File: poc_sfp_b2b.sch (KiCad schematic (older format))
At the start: 12 parts, among them J101 Barrel_Jack, Q101 Q_PMOS_DGS, U101 TPS62142

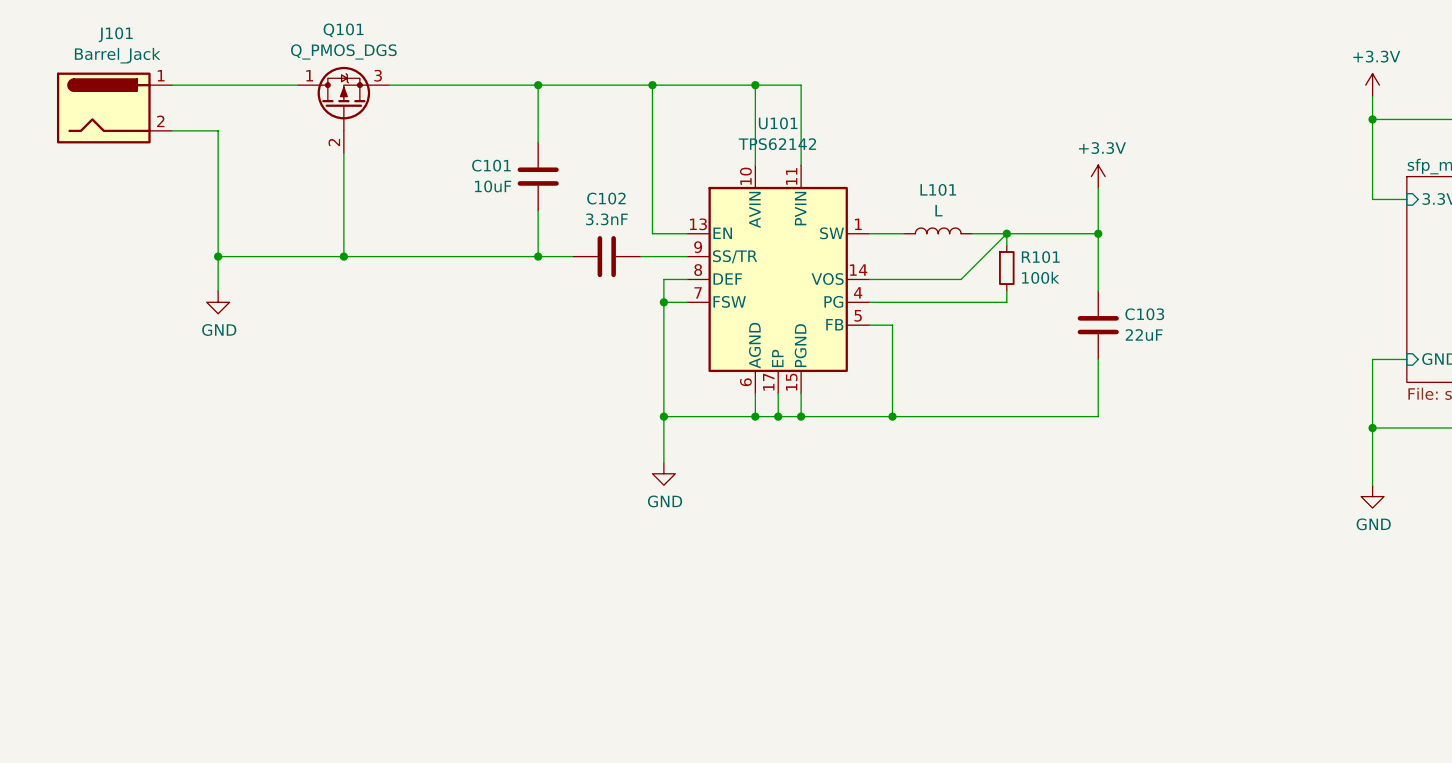
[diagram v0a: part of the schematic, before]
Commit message: fix unconnected tx disable pin
Signed-off-by: Thomas Schmid <tom@binary-kitchen.de>
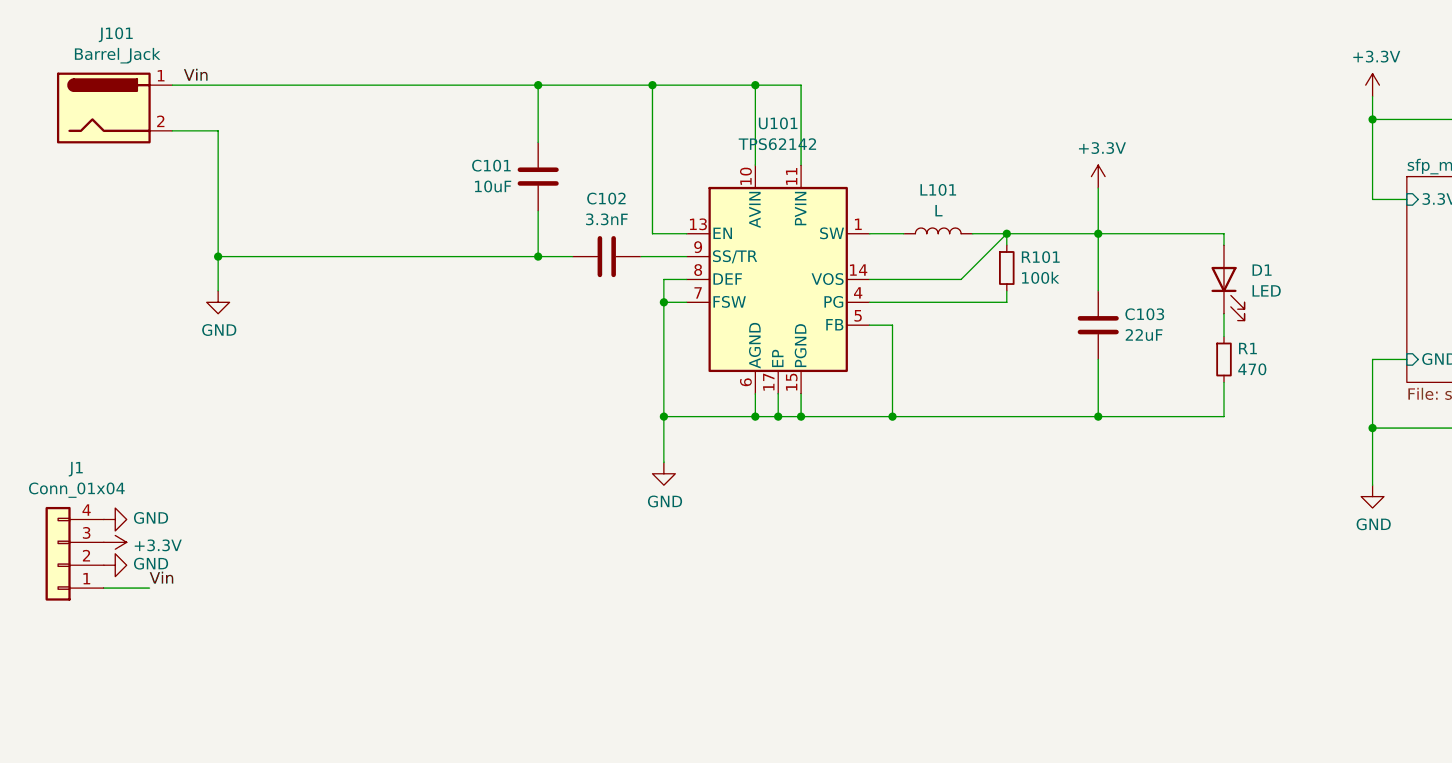
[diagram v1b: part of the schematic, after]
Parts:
- removed Q101: Q_PMOS_DGS, Package_SO:PowerPAK_SO-8_Single, symbol Device:Q_PMOS_DGS
- added D1: LED, LED_THT:LED_D3.0mm_Horizontal_O1.27mm_Z2.0mm, symbol Device:LED
- added J1: Conn_01x04, Connector_PinHeader_2.54mm:PinHeader_1x04_P2.54mm_Vertical, symbol Connector_Generic:Conn_01x04
- added R1: 470, Resistor_SMD:R_0805_2012Metric, symbol Device:R_Small
- C101: Mouser Link (none) -> https://www.mouser.de/ProductDetail/Samsung-Electro-Mechani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; Mouser Part Number (none) -> 187-CL32A106KAULNNE; Part Number (none) -> CL32A106KAULNNE
- C102: Mouser Link (none) -> https://www.mouser.de/ProductDetail/Yageo/CC0603KRX7R9BB332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; Mouser Part Number (none) -> 603-CC603KRX7R9BB332; Part Number (none) -> CC0603KRX7R9BB332
- C103: Mouser Link (none) -> https://www.mouser.de/ProductDetail/Samsung-Electro-Mechani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; Mouser Part Number (none) -> 187-CL21A226KQCLRNC; Part Number (none) -> CL21A226KQCLRNC
- J101: footprint Connector_BarrelJack:BarrelJack_CUI_PJ-063AH_Horizontal -> Connector_BarrelJack:BarrelJack_Horizontal; Mouser Link (none) -> https://www.mouser.de/ProductDetail/Gravitech/CON-SOCJ-2155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; Mouser Part Number (none) -> 992-CON-SOCJ-2155; Part Number (none) -> CON-SOCJ-2155
- L101: Mouser Link (none) -> https://www.mouser.de/ProductDetail/Coilcraft/XFL4020-222ME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; Mouser Part Number (none) -> 994-XFL4020-222MEB; Part Number (none) -> XFL4020-222MEB
- U101: Mouser Link (none) -> https://www.mouser.de/ProductDetail/Texas-Instruments/TPS62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; Mouser Part Number (none) -> 595-TPS62140ARGTR; Part Number (none) -> TPS62140ARGTR
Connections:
- net +3V3: now also D1.2 (A), J1.3 (Pin_3)
- net GND: now also J1.2 (Pin_2), J1.4 (Pin_4), R1.2
- net Vin: now reaches J101.1
- net Vin: now also C101.1, U101.10 (AVIN), U101.11 (PVIN), U101.12 (PVIN), U101.13 (EN), J1.1 (Pin_1)
- new net: D1.1 (K), R1.1
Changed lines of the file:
@@
 	6850 2850 6850 3200
-$Comp
-L Device:Q_PMOS_DGS Q101
-U 1 1 5F4B667B
-P 2350 2800
-F 0 "Q101" V 2692 2800 50  0000 C CNN
-F 1 "Q_PMOS_DGS" V 2601 2800 50  0000 C CNN
-F 2 "Package_SO:PowerPAK_SO-8_Single" H 2550 2900 50  0001 C CNN
-F 3 "~" H 2350 2800 50  0001 C CNN
-	1    2350 2800
-	0    -1   -1   0
-$EndComp
 $Comp
 L Connector:Barrel_Jack J101
@@
 F 0 "J101" H 1357 3125 50  0000 C CNN
 F 1 "Barrel_Jack" H 1357 3034 50  0000 C CNN
-F 2 "Connector_BarrelJack:BarrelJack_CUI_PJ-063AH_Horizontal" H 1350 2760 50  0001 C CNN
-F 3 "~" H 1350 2760 50  0001 C CNN
+F 2 "Connector_BarrelJack:BarrelJack_Horizontal" H 1350 2760 50  0001 C CNN
+F 3 "https://www.mouser.com/catalog/additional/Gravitech_CON_SOCJ_2155.jpg" H 1350 2760 50  0001 C CNN
+F 4 "https://www.mouser.de/ProductDetail/Gravitech/CON-SOCJ-2155?qs=fkzBJ5HM%252BdCcpvFQyQZHtA%3D%3D" H 1300 2800 50  0001 C CNN "Mouser Link"
+F 5 " 992-CON-SOCJ-2155 " H 1300 2800 50  0001 C CNN "Mouser Part Number"
+F 6 "CON-SOCJ-2155" H 1300 2800 50  0001 C CNN "Part Number"
 	1    1300 2800
 	1    0    0    -1
 $EndComp
 Wire Wire Line
-	1600 2700 2150 2700
-Wire Wire Line
 	1600 2900 1800 2900
 Wire Wire Line
 	1800 2900 1800 3450
-Wire Wire Line
-	1800 3450 2350 3450
-Wire Wire Line
-	2350 3450 2350 3000
 $Comp
 L power:GND #PWR0101
@@
 F 2 "Package_DFN_QFN:VQFN-16-1EP_3x3mm_P0.5mm_EP1.68x1.68mm_ThermalVias" H 4400 3100 50  0001 L CNN
 F 3 "http://www.ti.com/lit/ds/symlink/TPS62140.pdf" H 4250 3550 50  0001 C CNN
+F 4 "https://www.mouser.de/ProductDetail/Texas-Instruments/TPS62140ARGTR?qs=jGqriC4rmgu3kOXNaMklag%3D%3D" H 4250 3550 50  0001 C CNN "Mouser Link"
+F 5 "595-TPS62140ARGTR" H 4250 3550 50  0001 C CNN "Mouser Part Number"
+F 6 "TPS62140ARGTR" H 4250 3550 50  0001 C CNN "Part Number"
 	1    4250 3550
 	1    0    0    -1
 $EndComp
-Wire Wire Line
-	2550 2700 3200 2700
 Wire Wire Line
 	4150 2700 4150 3050
@@
 F 1 "10uF" H 3086 3055 50  0000 R CNN
 F 2 "Capacitor_SMD:C_1210_3225Metric" H 3238 2950 50  0001 C CNN
-F 3 "~" H 3200 3100 50  0001 C CNN
+F 3 "https://www.mouser.de/datasheet/2/585/MLCC-1837944.pdf" H 3200 3100 50  0001 C CNN
+F 4 "https://www.mouser.de/ProductDetail/Samsung-Electro-Mechanics/CL32A106KAULNNE?qs=X6jEic%2FHinC8rXXgzyw98Q%3D%3D" H 3200 3100 50  0001 C CNN "Mouser Link"
+F 5 "187-CL32A106KAULNNE" H 3200 3100 50  0001 C CNN "Mouser Part Number"
+F 6 "CL32A106KAULNNE" H 3200 3100 50  0001 C CNN "Part Number"
 	1    3200 3100
 	1    0    0    -1
@@
 F 1 "3.3nF" V 3339 3450 50  0000 C CNN
 F 2 "Capacitor_SMD:C_0603_1608Metric" H 3538 3300 50  0001 C CNN
-F 3 "~" H 3500 3450 50  0001 C CNN
+F 3 "https://www.mouser.de/datasheet/2/447/UPY-GPHC_X7R_6.3V-to-50V_18-1154002.pdf" H 3500 3450 50  0001 C CNN
+F 4 "https://www.mouser.de/ProductDetail/Yageo/CC0603KRX7R9BB332?qs=AgBp2OyFlx8UAnjSGzzw0Q%3D%3D" H 3500 3450 50  0001 C CNN "Mouser Link"
+F 5 "603-CC603KRX7R9BB332" H 3500 3450 50  0001 C CNN "Mouser Part Number"
+F 6 "CC0603KRX7R9BB332" H 3500 3450 50  0001 C CNN "Part Number"
 	1    3500 3450
 	0    1    1    0
@@
 Wire Wire Line
 	3200 3450 3200 3250
-Wire Wire Line
-	3200 3450 2350 3450
 Connection ~ 3200 3450
-Connection ~ 2350 3450
 Wire Wire Line
 	3200 3450 3350 3450
@@
 F 1 "L" V 5049 3350 50  0000 C CNN
 F 2 "Inductor_SMD:L_Coilcraft_XxL4020" H 4950 3350 50  0001 C CNN
-F 3 "~" H 4950 3350 50  0001 C CNN
+F 3 "https://www.mouser.de/datasheet/2/597/xfl4020-270756.pdf" H 4950 3350 50  0001 C CNN
+F 4 "https://www.mouser.de/ProductDetail/Coilcraft/XFL4020-222MEB?qs=VJjuEbE9QBO2bwonVBK1EA%3D%3D" H 4950 3350 50  0001 C CNN "Mouser Link"
+F 5 "994-XFL4020-222MEB" H 4950 3350 50  0001 C CNN "Mouser Part Number"
+F 6 "XFL4020-222MEB" H 4950 3350 50  0001 C CNN "Part Number"
 	1    4950 3350
 	0    -1   -1   0
@@
 F 1 "22uF" H 5765 3705 50  0000 L CNN
 F 2 "Capacitor_SMD:C_0805_2012Metric" H 5688 3600 50  0001 C CNN
-F 3 "~" H 5650 3750 50  0001 C CNN
+F 3 "https://www.mouser.de/datasheet/2/585/MLCC-1837944.pdf" H 5650 3750 50  0001 C CNN
+F 4 "https://www.mouser.de/ProductDetail/Samsung-Electro-Mechanics/CL21A226KQCLRNC?qs=xZ%2FP%252Ba9zWqYG0ePGTF%2FymQ%3D%3D" H 5650 3750 50  0001 C CNN "Mouser Link"
+F 5 "187-CL21A226KQCLRNC" H 5650 3750 50  0001 C CNN "Mouser Part Number"
+F 6 "CL21A226KQCLRNC" H 5650 3750 50  0001 C CNN "Part Number"
 	1    5650 3750
 	1    0    0    -1
@@
 	5650 4150 5650 3900
 Connection ~ 4750 4150
+$Comp
+L Device:LED D1
+U 1 1 5FC35AA3
+P 6200 3550
+F 0 "D1" V 6239 3432 50  0000 R CNN
+F 1 "LED" V 6148 3432 50  0000 R CNN
+F 2 "LED_THT:LED_D3.0mm_Horizontal_O1.27mm_Z2.0mm" H 6200 3550 50  0001 C CNN
+F 3 "~" H 6200 3550 50  0001 C CNN
+	1    6200 3550
+	0    -1   -1   0
+$EndComp
+$Comp
+L Device:R_Small R1
+U 1 1 5FC38121
+P 6200 3900
+F 0 "R1" H 6259 3946 50  0000 L CNN
+F 1 "470" H 6259 3855 50  0000 L CNN
+F 2 "Resistor_SMD:R_0805_2012Metric" H 6200 3900 50  0001 C CNN
+F 3 "~" H 6200 3900 50  0001 C CNN
+	1    6200 3900
+	1    0    0    -1
+$EndComp
+Wire Wire Line
+	5650 4150 6200 4150
+Wire Wire Line
+	6200 4150 6200 4000
+Connection ~ 5650 4150
+Wire Wire Line
+	6200 3800 6200 3700
+Wire Wire Line
+	6200 3400 6200 3350
+Wire Wire Line
+	6200 3350 5650 3350
+Wire Wire Line
+	1800 3450 3200 3450
+Wire Wire Line
+	1600 2700 3200 2700
+$Comp
+L Connector_Generic:Conn_01x04 J1
+U 1 1 5FC7A207
+P 1100 4800
+F 0 "J1" H 1018 4375 50  0000 C CNN
+F 1 "Conn_01x04" H 1018 4466 50  0000 C CNN
+F 2 "Connector_PinHeader_2.54mm:PinHeader_1x04_P2.54mm_Vertical" H 1100 4800 50  0001 C CNN
+F 3 "" H 1100 4800 50  0001 C CNN
+	1    1100 4800
+	-1   0    0    1
+$EndComp
+Text Label 1650 2700 0    50   ~ 0
+Vin
+Wire Wire Line
+	1300 4900 1500 4900
+$Comp
+L power:GND #PWR0107
+U 1 1 5FC80C27
+P 1300 4800
+F 0 "#PWR0107" H 1300 4550 50  0001 C CNN
+F 1 "GND" V 1305 4672 50  0000 R CNN
+F 2 "" H 1300 4800 50  0001 C CNN
+F 3 "" H 1300 4800 50  0001 C CNN
+	1    1300 4800
+	0    -1   -1   0
+$EndComp
+$Comp
+L power:+3.3V #PWR0108
+U 1 1 5FC81944
+P 1300 4700
+F 0 "#PWR0108" H 1300 4550 50  0001 C CNN
+F 1 "+3.3V" V 1315 4828 50  0000 L CNN
+F 2 "" H 1300 4700 50  0001 C CNN
+F 3 "" H 1300 4700 50  0001 C CNN
+	1    1300 4700
+	0    1    1    0
+$EndComp
+$Comp
+L power:GND #PWR0109
+U 1 1 5FC81F8A
+P 1300 4600
+F 0 "#PWR0109" H 1300 4350 50  0001 C CNN
+F 1 "GND" V 1305 4472 50  0000 R CNN
+F 2 "" H 1300 4600 50  0001 C CNN
+F 3 "" H 1300 4600 50  0001 C CNN
+	1    1300 4600
+	0    -1   -1   0
+$EndComp
+Text Label 1500 4900 0    50   ~ 0
+Vin
 $EndSCHEMATC
